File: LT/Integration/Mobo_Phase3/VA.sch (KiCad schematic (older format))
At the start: 25 parts, among them J2 Conn_Coaxial, U1 BAP64Q

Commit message: Fixed phase 3 integration folder for Mobo
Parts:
- U1: symbol Mobo_Dev1-rescue:BAP64Q-LT-Schematics -> Mobo_Phase3-rescue:BAP64Q-LT-Schematics
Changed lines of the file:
@@
 EESchema Schematic File Version 4
-LIBS:Mobo_Dev1-cache
+LIBS:Mobo_Phase3-cache
 EELAYER 26 0
 EELAYER END
@@
 $EndComp
 $Comp
-L Mobo_Dev1-rescue:BAP64Q-LT-Schematics U1
+L Mobo_Phase3-rescue:BAP64Q-LT-Schematics U1
 U 1 1 5E4E98DA
 P 7050 3300
-AR Path="/5E4E98DA" Ref="U1"  Part="1"
-AR Path="/5E9B72A2/5E4E98DA" Ref="U1"  Part="1"
 F 0 "U1" H 7150 3865 50  0000 C CNN
 F 1 "BAP64Q" H 7150 3774 50  0000 C CNN

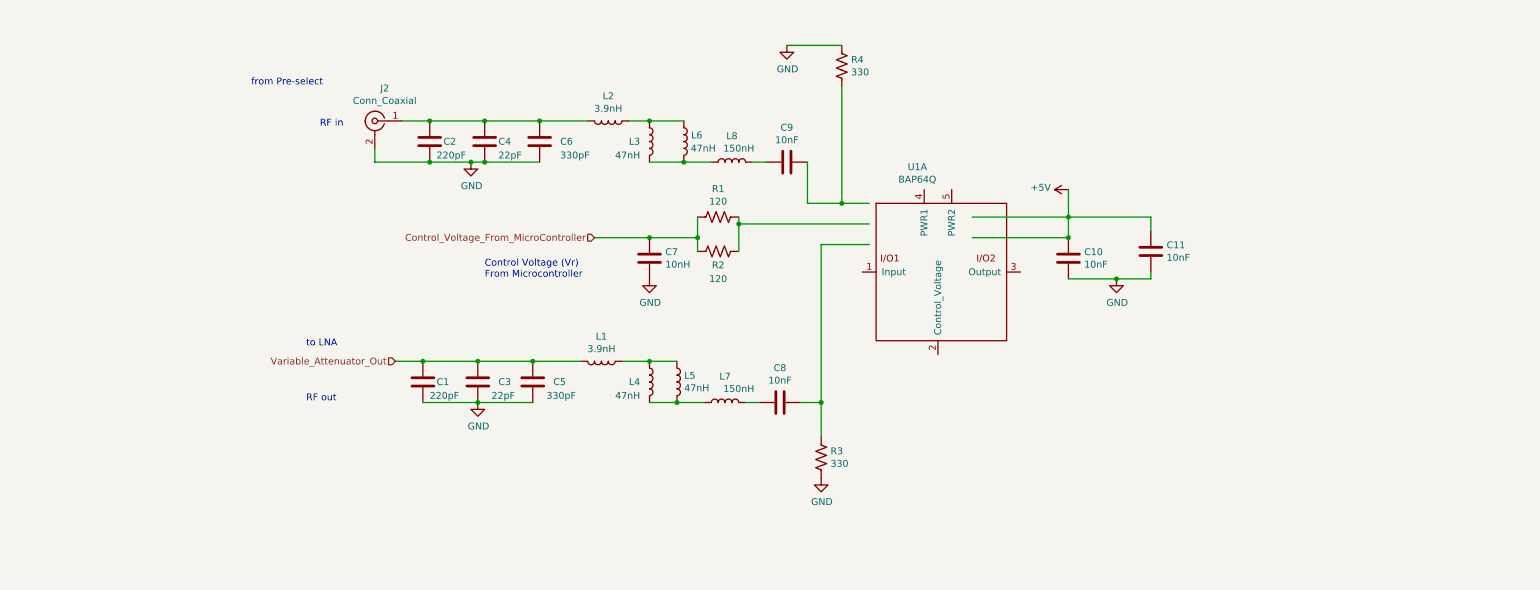
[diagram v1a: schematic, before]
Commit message: Finished the preliminary layout of the receiving stage for MoBo Phase 3
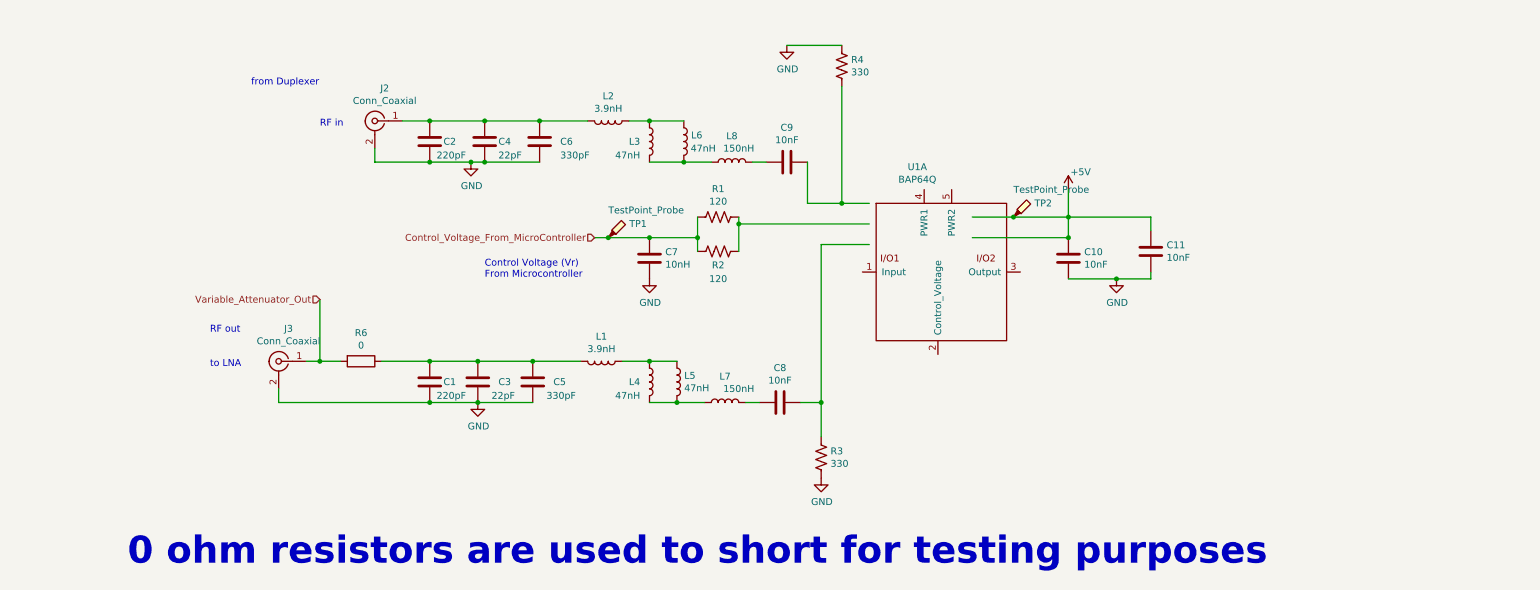
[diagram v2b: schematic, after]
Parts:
- added J3: Conn_Coaxial, Connector_Coaxial:SMA_Amphenol_132291_Vertical, symbol Connector:Conn_Coaxial
- added R6: 0, Resistor_SMD:R_0805_2012Metric_Pad1.15x1.40mm_HandSolder, symbol Device:R
- added TP1: TestPoint_Probe, TestPoint:TestPoint_Pad_D1.5mm, symbol Connector:TestPoint_Probe
- added TP2: TestPoint_Probe, TestPoint:TestPoint_Plated_Hole_D2.0mm, symbol Connector:TestPoint_Probe
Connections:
- wire segments 50 -> 57
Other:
- note added: "0 ohm resistors are used to short for testing purposes"
- note added: "from Duplexer"
- note removed: "from Pre-select"
- moved on the sheet: C1
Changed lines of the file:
@@
 EESchema Schematic File Version 4
-LIBS:Mobo_Phase3-cache
-EELAYER 26 0
+EELAYER 30 0
 EELAYER END
 $Descr A4 11693 8268
@@
 L Device:C C1
 U 1 1 5E4FD576
-P 3550 4300
-F 0 "C1" H 3650 4300 50  0000 L CNN
-F 1 "220pF" H 3600 4200 50  0000 L CNN
-F 2 "Capacitor_SMD:C_0402_1005Metric" H 3588 4150 50  0001 C CNN
-F 3 "~" H 3550 4300 50  0001 C CNN
-	1    3550 4300
+P 3600 4300
+F 0 "C1" H 3700 4300 50  0000 L CNN
+F 1 "220pF" H 3650 4200 50  0000 L CNN
+F 2 "Capacitor_SMD:C_0402_1005Metric" H 3638 4150 50  0001 C CNN
+F 3 "~" H 3600 4300 50  0001 C CNN
+	1    3600 4300
 	1    0    0    -1
 $EndComp
@@
 $EndComp
 Wire Wire Line
-	3350 4150 3550 4150
-Connection ~ 3550 4150
-Wire Wire Line
-	3550 4150 3950 4150
+	3600 4150 3950 4150
 Connection ~ 3950 4150
 Wire Wire Line
@@
 Text Notes 2800 2450 0    50   ~ 0
 RF in
-Text Notes 2700 4450 0    50   ~ 0
+Text Notes 2000 3950 0    50   ~ 0
 RF out
 Wire Wire Line
@@
 	3950 4450 4350 4450
 Wire Wire Line
-	7550 3100 8250 3100
+	7550 3100 7850 3100
 Wire Wire Line
 	8250 3100 8250 2900
-Wire Wire Line
-	8250 3100 8850 3100
 Wire Wire Line
 	8850 3100 8850 3200
@@
 P 8250 2900
 F 0 "#PWR06" H 8250 2750 50  0001 C CNN
-F 1 "+5V" V 8265 3028 50  0000 L CNN
+F 1 "+5V" H 8265 3028 50  0000 L CNN
 F 2 "" H 8250 2900 50  0001 C CNN
 F 3 "" H 8250 2900 50  0001 C CNN
 	1    8250 2900
-	0    -1   -1   0
+	1    0    0    -1
 $EndComp
 Wire Wire Line
@@
 $EndComp
 Text Notes 2300 2150 0    50   ~ 0
-from Pre-select
-Text Notes 2700 4050 0    50   ~ 0
+from Duplexer
+Text Notes 2000 4200 0    50   ~ 0
 to LNA
 Wire Wire Line
-	3550 4450 3950 4450
+	3600 4450 3950 4450
 Wire Wire Line
 	5050 2400 5200 2400
@@
 	5200 4450 5400 4450
 Connection ~ 5400 4450
-Text HLabel 3350 4150 0    50   Input ~ 0
+Text HLabel 2800 3700 0    50   Input ~ 0
 Variable_Attenuator_Out
 $Comp
@@
 Connection ~ 5200 3250
 Wire Wire Line
-	4800 3250 5200 3250
+	4800 3250 4900 3250
 Text Notes 4000 3550 0    50   ~ 0
 Control Voltage (Vr)\nFrom Microcontroller
 Text HLabel 4800 3250 0    50   Input ~ 0
 Control_Voltage_From_MicroController
+$Comp
+L Device:R R6
+U 1 1 5EB1ED68
+P 3100 4150
+F 0 "R6" V 2893 4150 50  0000 C CNN
+F 1 "0" V 2984 4150 50  0000 C CNN
+F 2 "Resistor_SMD:R_0805_2012Metric_Pad1.15x1.40mm_HandSolder" V 3030 4150 50  0001 C CNN
+F 3 "~" H 3100 4150 50  0001 C CNN
+	1    3100 4150
+	0    1    1    0
+$EndComp
+Connection ~ 3600 4150
+$Comp
+L Connector:Conn_Coaxial J3
+U 1 1 5EB28989
+P 2500 4150
+F 0 "J3" H 2428 4388 50  0000 C CNN
+F 1 "Conn_Coaxial" H 2428 4297 50  0000 C CNN
+F 2 "Connector_Coaxial:SMA_Amphenol_132291_Vertical" H 2500 4150 50  0001 C CNN
+F 3 " ~" H 2500 4150 50  0001 C CNN
+	1    2500 4150
+	-1   0    0    -1
+$EndComp
+Wire Wire Line
+	2800 3700 2800 4150
+Wire Wire Line
+	2700 4150 2800 4150
+Connection ~ 2800 4150
+Wire Wire Line
+	2800 4150 2950 4150
+Wire Wire Line
+	2500 4350 2500 4450
+Wire Wire Line
+	2500 4450 3600 4450
+Connection ~ 3600 4450
+Text Notes 1400 5650 0    197  ~ 39
+0 ohm resistors are used to short for testing purposes
+$Comp
+L Connector:TestPoint_Probe TP2
+U 1 1 5EB433E7
+P 7850 3100
+F 0 "TP2" H 8003 3201 50  0000 L CNN
+F 1 "TestPoint_Probe" H 7850 3300 50  0000 L CNN
+F 2 "TestPoint:TestPoint_Plated_Hole_D2.0mm" H 8050 3100 50  0001 C CNN
+F 3 "~" H 8050 3100 50  0001 C CNN
+	1    7850 3100
+	1    0    0    -1
+$EndComp
+$Comp
+L Connector:TestPoint_Probe TP1
+U 1 1 5EB460CF
+P 4900 3250
+F 0 "TP1" H 5053 3351 50  0000 L CNN
+F 1 "TestPoint_Probe" H 4900 3450 50  0000 L CNN
+F 2 "TestPoint:TestPoint_Pad_D1.5mm" H 5100 3250 50  0001 C CNN
+F 3 "~" H 5100 3250 50  0001 C CNN
+	1    4900 3250
+	1    0    0    -1
+$EndComp
+Connection ~ 4900 3250
+Wire Wire Line
+	4900 3250 5200 3250
+Wire Wire Line
+	3250 4150 3600 4150
+Connection ~ 7850 3100
+Wire Wire Line
+	7850 3100 8250 3100
+Wire Wire Line
+	8250 3100 8850 3100
 $EndSCHEMATC

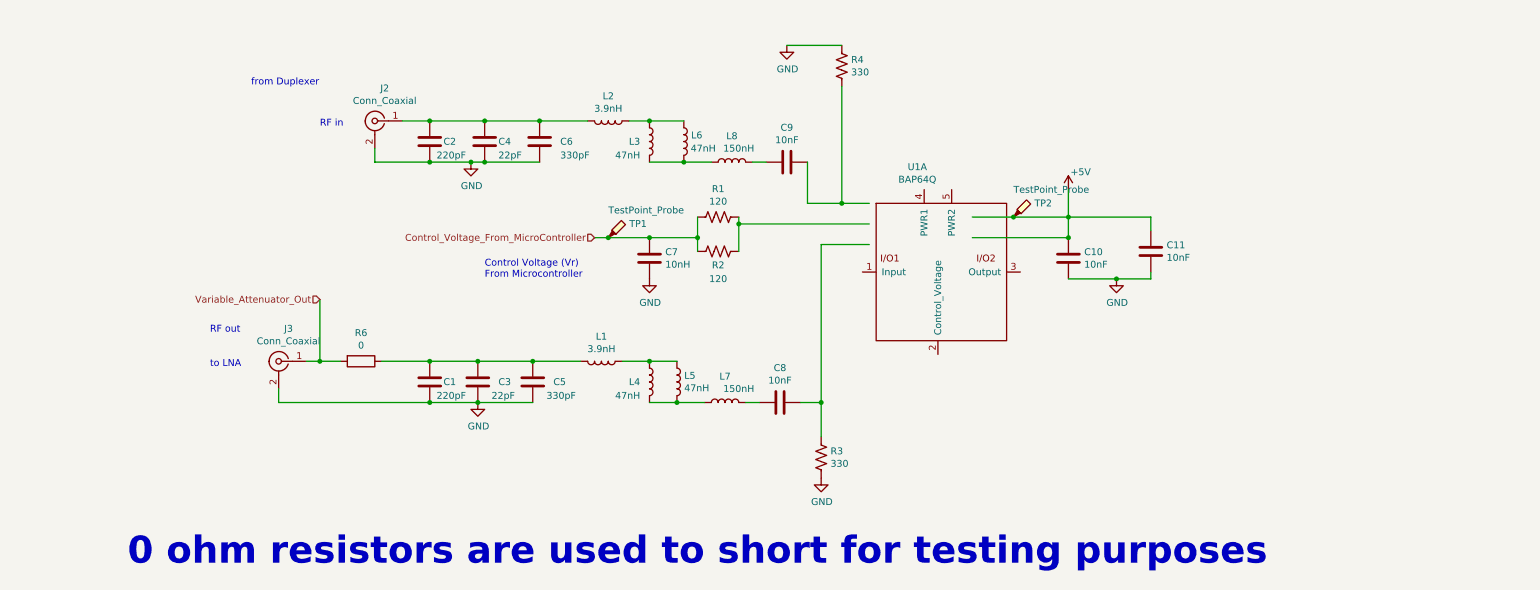
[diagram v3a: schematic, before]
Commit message: Fixed the hierarchy for the MoBo Phase 3
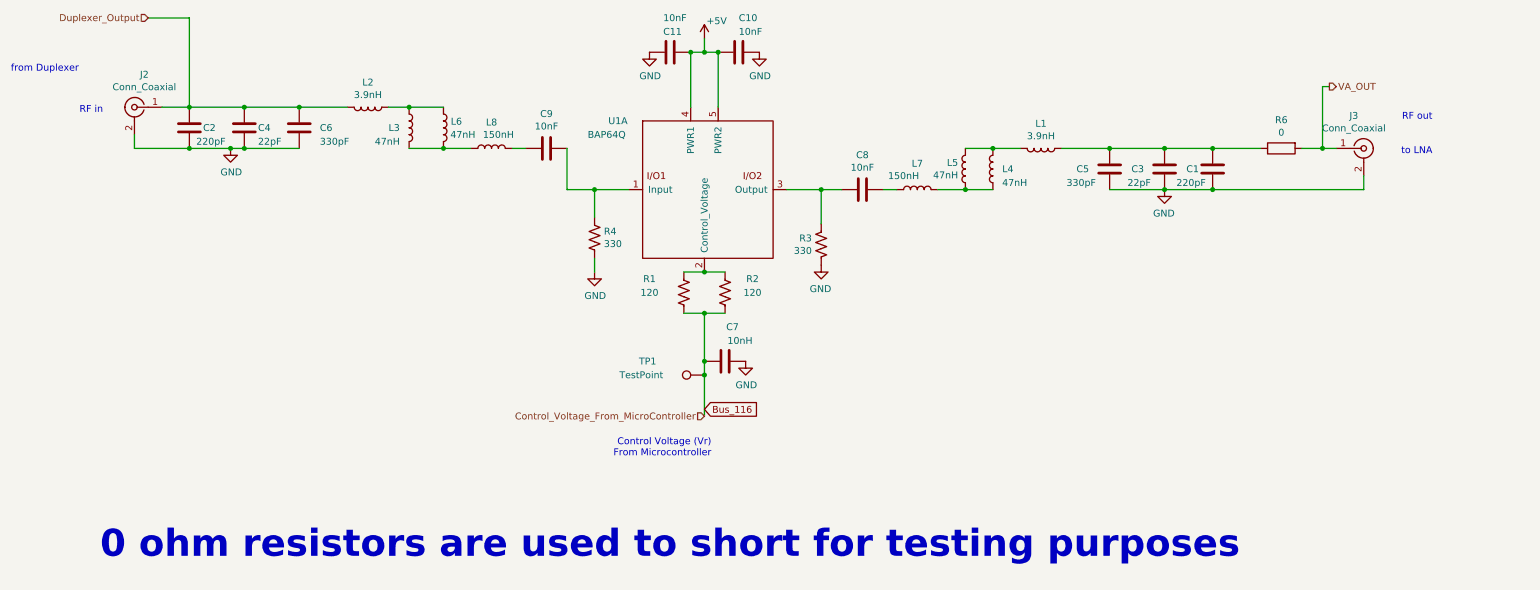
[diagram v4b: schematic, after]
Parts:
- removed TP1: TestPoint_Probe, TestPoint:TestPoint_Pad_D1.5mm, symbol Connector:TestPoint_Probe
- removed TP2: TestPoint_Probe, TestPoint:TestPoint_Plated_Hole_D2.0mm, symbol Connector:TestPoint_Probe
- added TP1: TestPoint, TestPoint:TestPoint_Pad_D1.5mm, symbol Connector:TestPoint
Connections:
- net labels added: Bus_116, Duplexer_Output, VA_OUT
- net labels removed: Variable_Attenuator_Out
- wire segments 57 -> 53
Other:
- moved on the sheet: C1, C10, C11, C2, C3, C4, C5, C6, C7, C8, C9, J2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

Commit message: Added the finalized layouts for the Mobo and Dobo Phase 3, as well as the preliminary layout for Phase 4 of both boards
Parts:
- J2: footprint Connector_Coaxial:SMA_Amphenol_132289_EdgeMount -> Connector_Coaxial:SMA_Amphenol_132291_Vertical
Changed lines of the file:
@@
 F 0 "J2" H 1378 2538 50  0000 C CNN
 F 1 "Conn_Coaxial" H 1378 2447 50  0000 C CNN
-F 2 "Connector_Coaxial:SMA_Amphenol_132289_EdgeMount" H 1450 2300 50  0001 C CNN
+F 2 "Connector_Coaxial:SMA_Amphenol_132291_Vertical" H 1450 2300 50  0001 C CNN
 F 3 " ~" H 1450 2300 50  0001 C CNN
 	1    1450 2300
